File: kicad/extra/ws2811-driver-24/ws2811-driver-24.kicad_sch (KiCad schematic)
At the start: 18 parts, among them J1 Conn_01x13_Pin, J2 Conn_01x13_Pin, J3 RJ45 IN, J4 RJ45 OUT, J5 Conn_01x03_Pin, U1 WS2811, U2 WS2811, U3 WS2811, U4 WS2811, U5 WS2811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

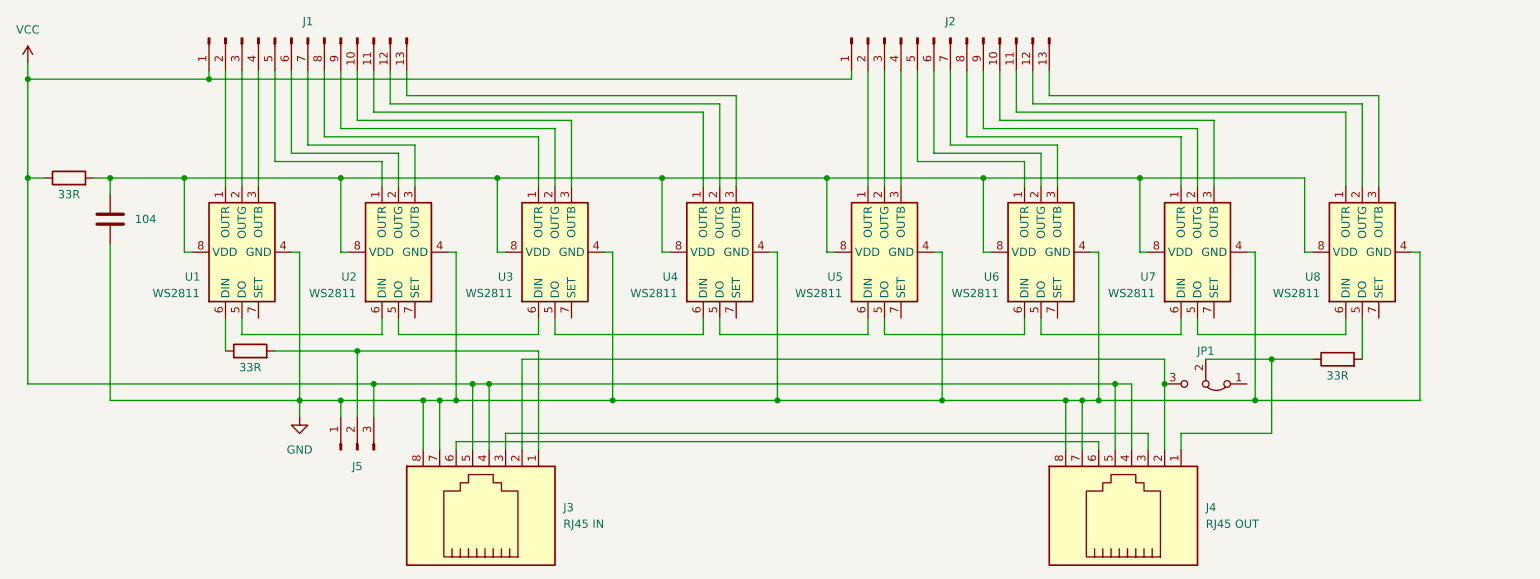
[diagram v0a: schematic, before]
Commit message: feat: Rework WS2811 boards (Rev 2.0)
* Change RJ45 pinout: The data signal is always paired with a ground
  line to increase signal stability, and the changed wireing eases the
  traces on the boards.

* All WS2811 driver boards have a three pin header for direct drive now.
  They can be directly connected to a signal decoder, e.g. for testing.

* The adapter boards has jumper pins to bypass RJ45 jacks, in case you
  want to connect another board using the final pin header.

* Change pin header component to a better available JCSC parts number.

* Move RJ45 jacks on driver boards a bit more off the board, so that
  there is less space between the jack and the outer side of the Watti
  carrier. This makes it easier to plug in and out RJ45 cables as
  the latches are easier to reach.

Fixes #4
Fixes #5
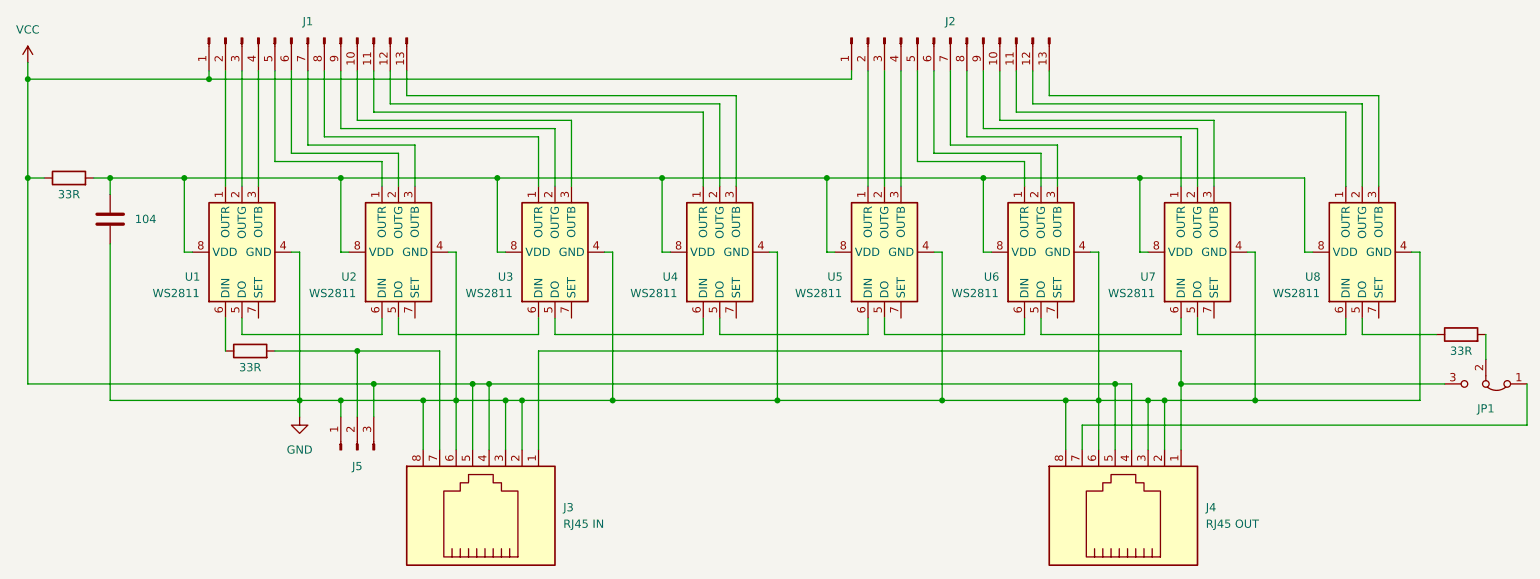
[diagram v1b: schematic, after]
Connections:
- net GND: now also J3.2, J3.3, J3.6, J4.2, J4.3, J4.6; no longer J3.7, J4.7
- net at U8.5 (DO): now also R3.1; no longer R3.2
- net at J5.2 (Pin_2), R2.2: now also J3.7; no longer J3.1
- net at JP1.1 (A): now also J4.7
- new net: JP1.2 (C), R3.2
- new net: J3.1, J4.1, JP1.3 (B)
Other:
- title: WS2811 LED Driver 24 (2 Signal) -> WS2811 LED Driver 24 (2 Signals)
- moved on the sheet: JP1
